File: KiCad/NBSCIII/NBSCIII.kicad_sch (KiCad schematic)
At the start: 9 parts, among them P1 CONN_1, P2 CONN_1, P3 CONN_1, P4 CONN_1

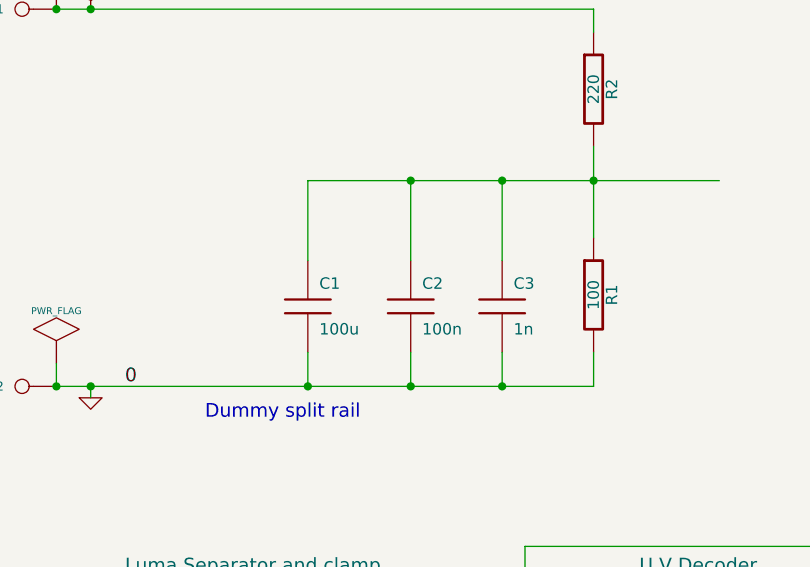
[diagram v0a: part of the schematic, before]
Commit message: unrescue to Device:C
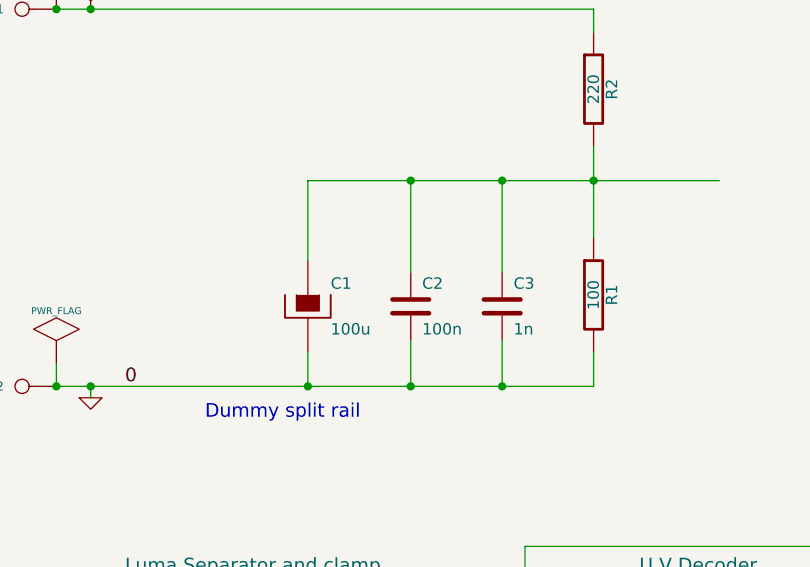
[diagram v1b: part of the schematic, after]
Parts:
- removed C1: 100u, symbol NBSCIII-rescue:C
- added C1: 100u, symbol NBSCIII-rescue:CP
- C2, C3: symbol NBSCIII-rescue:C -> Device:C
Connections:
- net GND: now also C1.2
- net at C2.1, C3.1, R1.1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: now also C1.1
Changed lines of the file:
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@@
   )
   (no_connect (at 148.59 153.67))
-  (wire (pts (xy 59.69 57.15) (xy 59.69 48.26))
+  (wire (pts (xy 59.69 48.26) (xy 59.69 57.15))
     (stroke (width 0) (type default) (color 0 0 0 0))
   )
@@
     (stroke (width 0) (type default) (color 0 0 0 0))
   )
+  (wire (pts (xy 59.69 67.31) (xy 59.69 71.12))
+    (stroke (width 0) (type default) (color 0 0 0 0))
+  )
   (wire (pts (xy 152.4 102.87) (xy 152.4 111.76))
     (stroke (width 0) (type default) (color 0 0 0 0))
@@
     (stroke (width 0) (type default) (color 0 0 0 0))
   )
-  (wire (pts (xy 81.28 71.12) (xy 81.28 67.31))
+  (wire (pts (xy 81.28 66.04) (xy 81.28 71.12))
     (stroke (width 0) (type default) (color 0 0 0 0))
   )
@@
     (stroke (width 0) (type default) (color 0 0 0 0))
   )
-  (wire (pts (xy 81.28 48.26) (xy 81.28 57.15))
+  (wire (pts (xy 81.28 48.26) (xy 81.28 58.42))
     (stroke (width 0) (type default) (color 0 0 0 0))
   )
@@
     (stroke (width 0) (type default) (color 0 0 0 0))
   )
-  (wire (pts (xy 59.69 67.31) (xy 59.69 71.12))
-    (stroke (width 0) (type default) (color 0 0 0 0))
-  )
   (wire (pts (xy 166.37 95.25) (xy 156.21 95.25))
     (stroke (width 0) (type default) (color 0 0 0 0))
@@
     (stroke (width 0) (type default) (color 0 0 0 0))
   )
+  (wire (pts (xy 71.12 66.04) (xy 71.12 71.12))
+    (stroke (width 0) (type default) (color 0 0 0 0))
+  )
   (wire (pts (xy 39.37 104.14) (xy 27.94 104.14))
     (stroke (width 0) (type default) (color 0 0 0 0))
@@
     (stroke (width 0) (type default) (color 0 0 0 0))
   )
-  (wire (pts (xy 71.12 71.12) (xy 71.12 67.31))
-    (stroke (width 0) (type default) (color 0 0 0 0))
-  )
   (wire (pts (xy 85.09 116.84) (xy 96.52 116.84))
     (stroke (width 0) (type default) (color 0 0 0 0))
@@
     (stroke (width 0) (type default) (color 0 0 0 0))
   )
-  (wire (pts (xy 71.12 48.26) (xy 71.12 57.15))
-    (stroke (width 0) (type default) (color 0 0 0 0))
-  )
   (wire (pts (xy 146.05 128.27) (xy 146.05 143.51))
     (stroke (width 0) (type default) (color 0 0 0 0))
@@
   )
   (wire (pts (xy 166.37 99.06) (xy 156.21 99.06))
+    (stroke (width 0) (type default) (color 0 0 0 0))
+  )
+  (wire (pts (xy 71.12 48.26) (xy 71.12 58.42))
     (stroke (width 0) (type default) (color 0 0 0 0))
   )
@@
     (pin "2")
   )
-  (symbol (lib_id "NBSCIII-rescue:C") (at 81.28 62.23 0) (unit 1)
+  (symbol (lib_id "Device:C") (at 81.28 62.23 0) (unit 1)
     (in_bom yes) (on_board yes)
     (property "Reference" "C3" (id 0) (at 82.55 59.69 0)
@@
     (pin "2")
   )
-  (symbol (lib_id "NBSCIII-rescue:C") (at 71.12 62.23 0) (unit 1)
+  (symbol (lib_id "Device:C") (at 71.12 62.23 0) (unit 1)
     (in_bom yes) (on_board yes)
     (property "Reference" "C2" (id 0) (at 72.39 59.69 0)
@@
     (pin "2")
   )
-  (symbol (lib_id "NBSCIII-rescue:C") (at 59.69 62.23 0) (unit 1)
-    (in_bom yes) (on_board yes)
-    (property "Reference" "C1" (id 0) (at 60.96 59.69 0)
-      (effects (font (size 1.27 1.27)) (justify left))
-    )
-    (property "Value" "100u" (id 1) (at 60.96 64.77 0)
-      (effects (font (size 1.27 1.27)) (justify left))
-    )
-    (property "Footprint" "" (id 2) (at 59.69 62.23 0)
-      (effects (font (size 1.27 1.27)) hide)
-    )
-    (property "Datasheet" "" (id 3) (at 59.69 62.23 0)
-      (effects (font (size 1.27 1.27)) hide)
-    )
-    (pin "1")
-    (pin "2")
-  )
   (symbol (lib_id "NBSCIII-rescue:GND") (at 35.56 72.39 0) (unit 1)
     (in_bom yes) (on_board yes)
@@
     )
     (pin "1")
+  )
+  (symbol (lib_id "NBSCIII-rescue:CP") (at 59.69 62.23 0) (unit 1)
+    (in_bom yes) (on_board yes)
+    (property "Reference" "C1" (id 0) (at 62.23 59.69 0)
+      (effects (font (size 1.27 1.27)) (justify left))
+    )
+    (property "Value" "100u" (id 1) (at 62.23 64.77 0)
+      (effects (font (size 1.27 1.27)) (justify left))
+    )
+    (property "Footprint" "" (id 2) (at 59.69 62.23 0)
+      (effects (font (size 1.27 1.27)) hide)
+    )
+    (property "Datasheet" "" (id 3) (at 59.69 62.23 0)
+      (effects (font (size 1.27 1.27)) hide)
+    )
+    (pin "1")
+    (pin "2")
   )
   (sheet (at 166.37 92.71) (size 43.18 29.21) (fields_autoplaced)
@@
       (reference "3k3") (unit 1) (value "R1000") (footprint "")
     )
-    (path "/00000000-0000-0000-0000-0000490732da"
+    (path "/ac188669-dbb6-4172-80c6-d06ada54efd8"
       (reference "C1") (unit 1) (value "100u") (footprint "")
     )

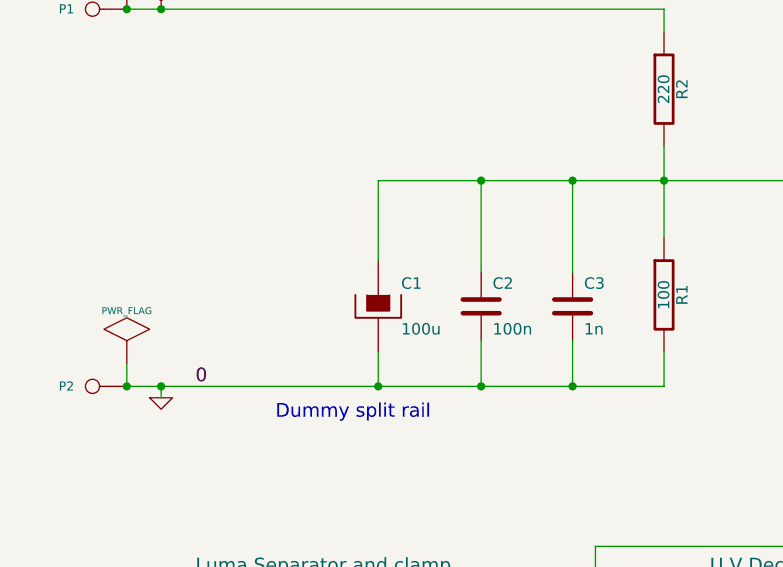
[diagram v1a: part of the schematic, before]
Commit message: unrescue to Device:C_Polarized
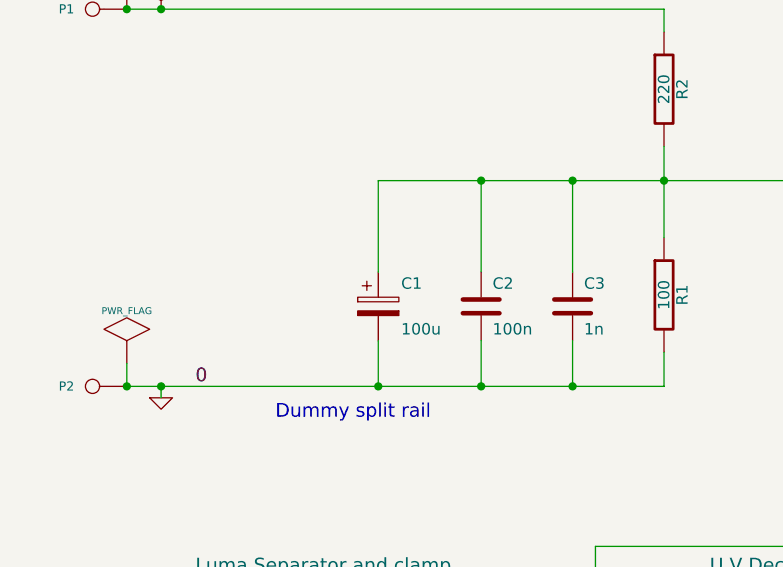
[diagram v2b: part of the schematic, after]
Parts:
- C1: symbol NBSCIII-rescue:CP -> Device:C_Polarized
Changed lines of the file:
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@@
   )
   (no_connect (at 148.59 153.67))
-  (wire (pts (xy 59.69 48.26) (xy 59.69 57.15))
+  (wire (pts (xy 59.69 48.26) (xy 59.69 58.42))
     (stroke (width 0) (type default) (color 0 0 0 0))
   )
@@
     (stroke (width 0) (type default) (color 0 0 0 0))
   )
-  (wire (pts (xy 59.69 67.31) (xy 59.69 71.12))
+  (wire (pts (xy 59.69 66.04) (xy 59.69 71.12))
     (stroke (width 0) (type default) (color 0 0 0 0))
   )
@@
     (pin "1")
   )
-  (symbol (lib_id "NBSCIII-rescue:CP") (at 59.69 62.23 0) (unit 1)
+  (symbol (lib_id "Device:C_Polarized") (at 59.69 62.23 0) (unit 1)
     (in_bom yes) (on_board yes)
     (property "Reference" "C1" (id 0) (at 62.23 59.69 0)

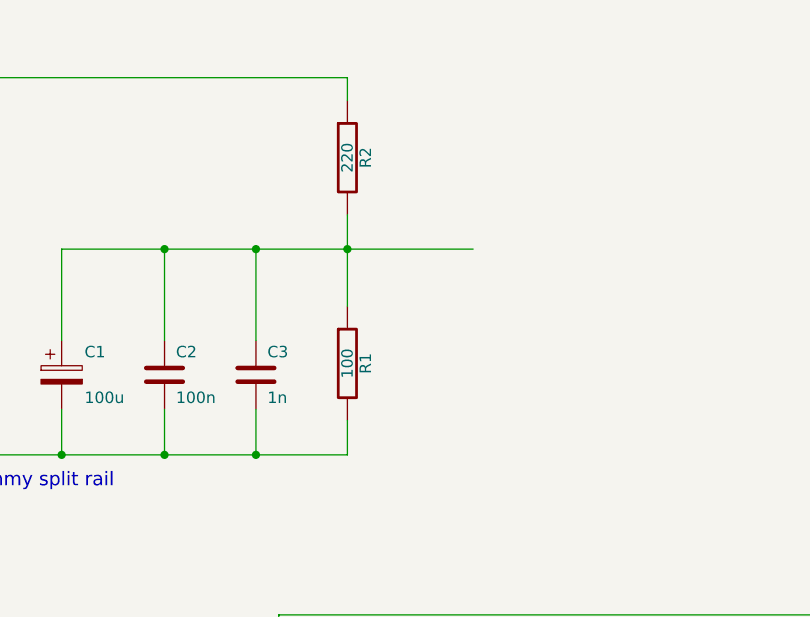
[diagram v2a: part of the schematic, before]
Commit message: unrescue Device:R
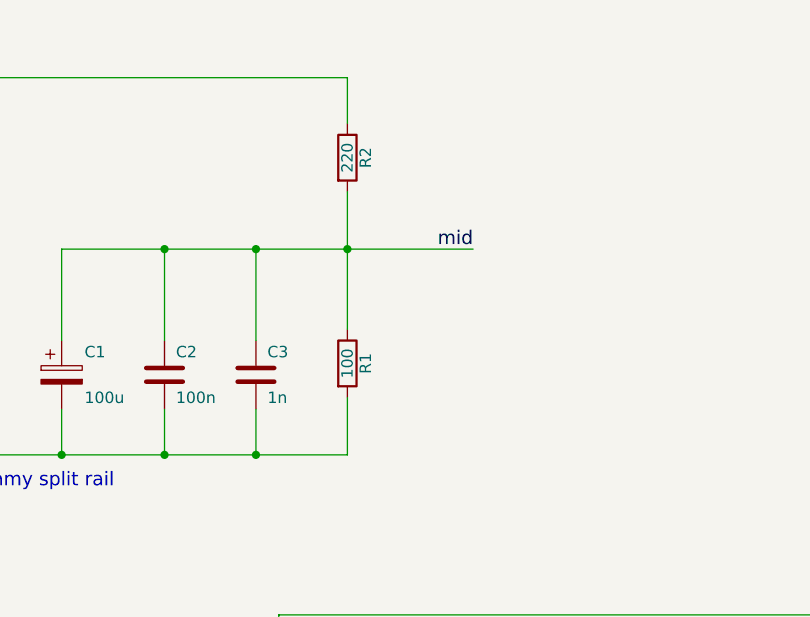
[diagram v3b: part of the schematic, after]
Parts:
- R1, R2: symbol NBSCIII-rescue:R -> Device:R
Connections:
- net mid: now also C1.1, C2.1, C3.1, R1.1, R2.2
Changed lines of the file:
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@@
     (stroke (width 0) (type default) (color 0 0 0 0))
   )
-  (wire (pts (xy 91.44 44.45) (xy 91.44 48.26))
+  (wire (pts (xy 91.44 41.91) (xy 91.44 48.26))
     (stroke (width 0) (type default) (color 0 0 0 0))
   )
@@
     (stroke (width 0) (type default) (color 0 0 0 0))
   )
-  (wire (pts (xy 91.44 48.26) (xy 91.44 54.61))
+  (wire (pts (xy 91.44 48.26) (xy 91.44 57.15))
     (stroke (width 0) (type default) (color 0 0 0 0))
   )
@@
     (stroke (width 0) (type default) (color 0 0 0 0))
   )
-  (wire (pts (xy 91.44 67.31) (xy 91.44 71.12))
+  (wire (pts (xy 91.44 64.77) (xy 91.44 71.12))
     (stroke (width 0) (type default) (color 0 0 0 0))
   )
@@
     (stroke (width 0) (type default) (color 0 0 0 0))
   )
-  (wire (pts (xy 91.44 31.75) (xy 91.44 29.21))
+  (wire (pts (xy 91.44 29.21) (xy 91.44 34.29))
     (stroke (width 0) (type default) (color 0 0 0 0))
   )
@@
     (effects (font (size 1.524 1.524)) (justify left bottom))
   )
+  (label "mid" (at 105.41 48.26 180)
+    (effects (font (size 1.524 1.524)) (justify right bottom))
+  )
   (label "mid" (at 158.75 101.6 0)
     (effects (font (size 1.524 1.524)) (justify left bottom))
@@
     (effects (font (size 1.524 1.524)) (justify left bottom))
   )
-  (symbol (lib_id "NBSCIII-rescue:R") (at 91.44 38.1 0) (unit 1)
+  (symbol (lib_id "Device:R") (at 91.44 38.1 0) (unit 1)
     (in_bom yes) (on_board yes)
     (property "Reference" "R2" (id 0) (at 93.472 38.1 90))
@@
     (pin "2")
   )
-  (symbol (lib_id "NBSCIII-rescue:R") (at 91.44 60.96 0) (unit 1)
+  (symbol (lib_id "Device:R") (at 91.44 60.96 0) (unit 1)
     (in_bom yes) (on_board yes)
     (property "Reference" "R1" (id 0) (at 93.472 60.96 90))

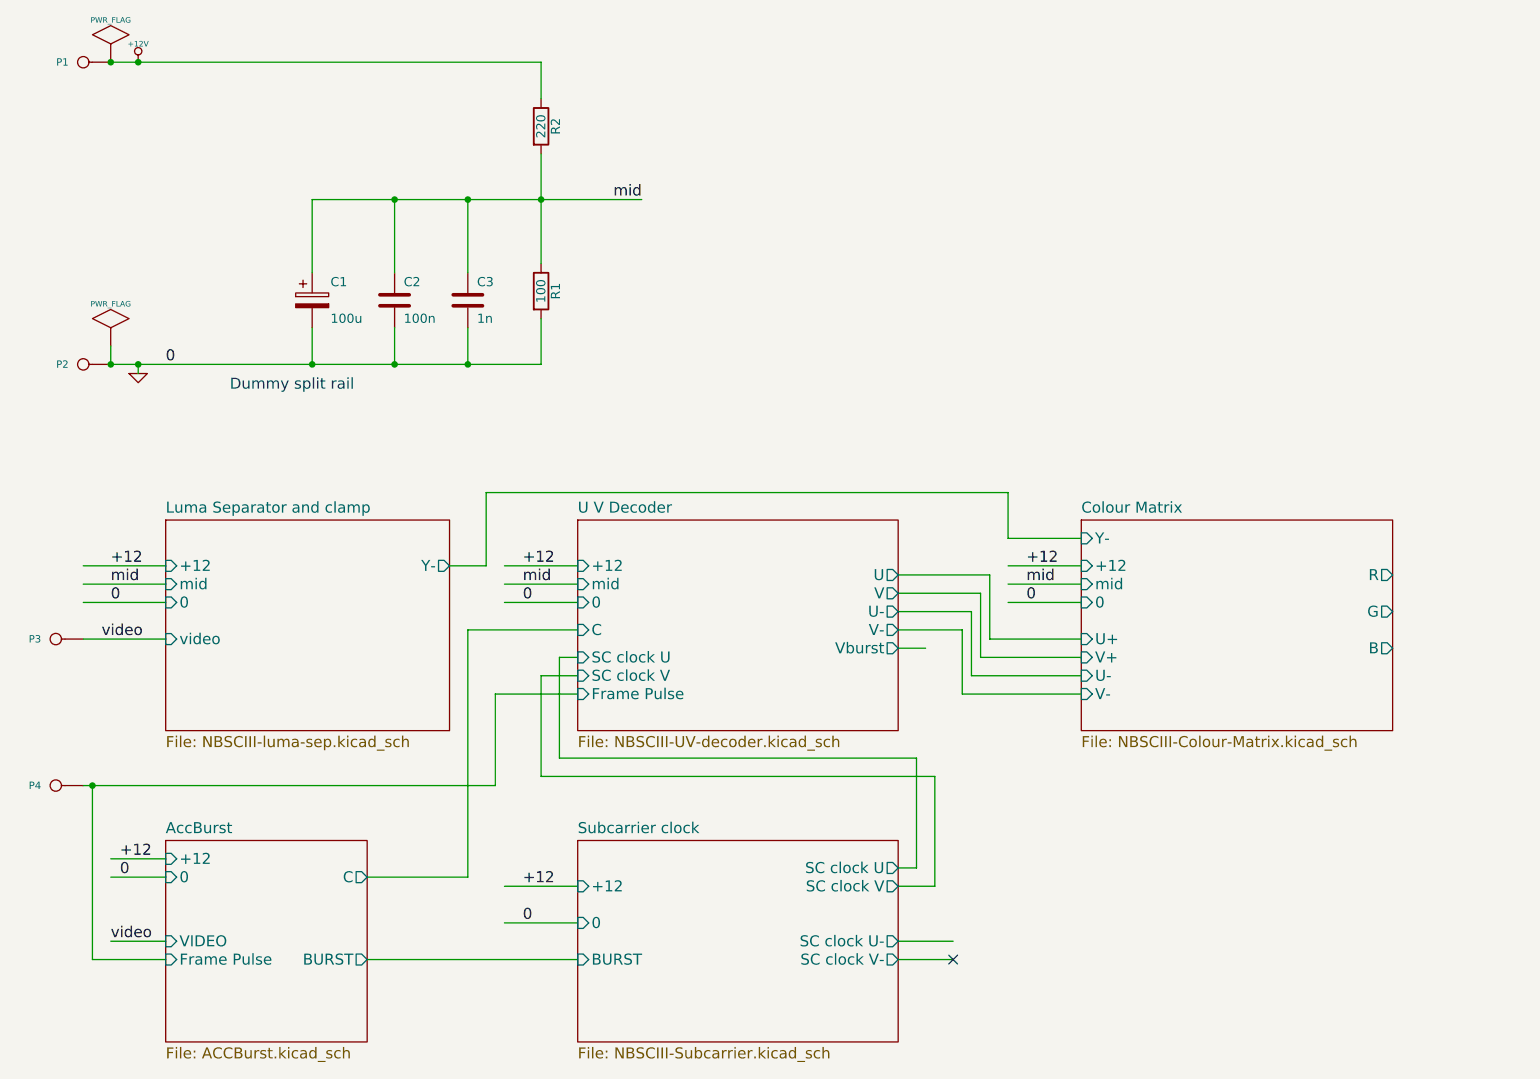
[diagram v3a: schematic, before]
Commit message: Simplify power distribution and make global
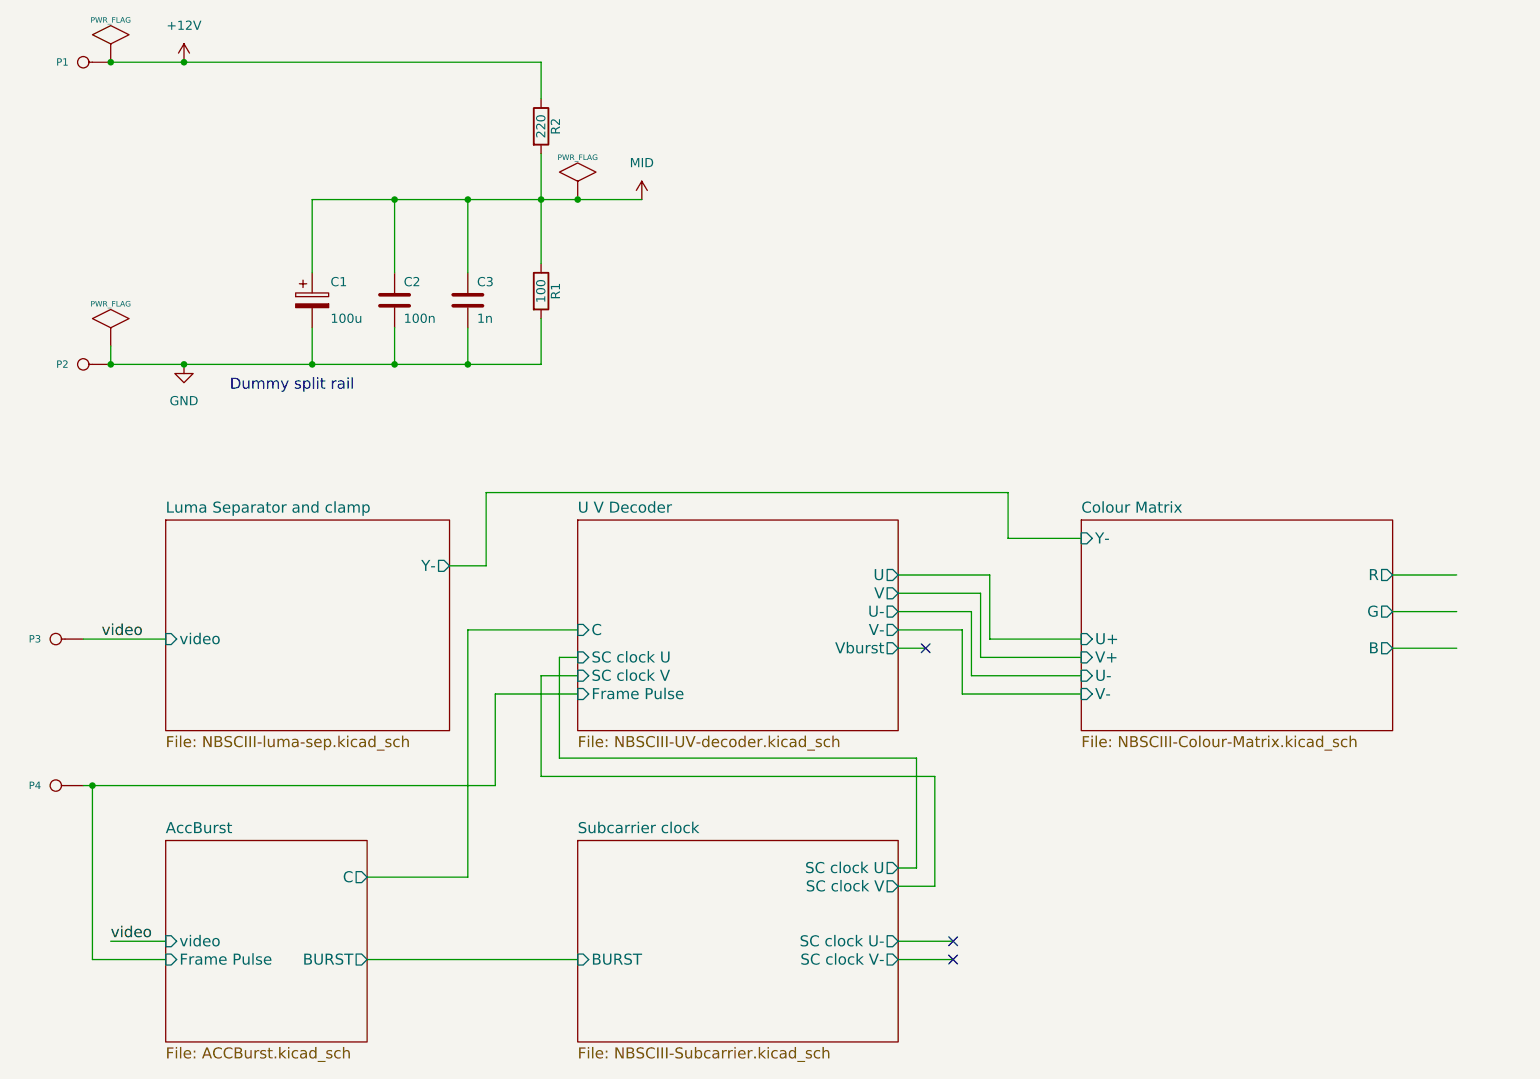
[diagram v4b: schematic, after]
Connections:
- net mid renamed MID
- no-connect marks 1 -> 3
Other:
- sheet AccBurst ports: added video; removed +12, 0, VIDEO
- sheet Colour Matrix ports: added none; removed +12, 0, mid
- sheet Luma Separator and clamp ports: added none; removed +12, 0, mid
- sheet Subcarrier clock ports: added none; removed +12, 0
- sheet U V Decoder ports: added none; removed +12, 0, mid
